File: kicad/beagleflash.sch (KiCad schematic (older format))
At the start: 22 parts, among them P1 SPI-8, P2 SPI-16, P3 BBB_P9, P4 BBB_P8, P5 EEPROM_PROG_EN, SW1 DIPS_02, U1 PAM2305AAB330, U2 74HC125, U3 CAT24C256W

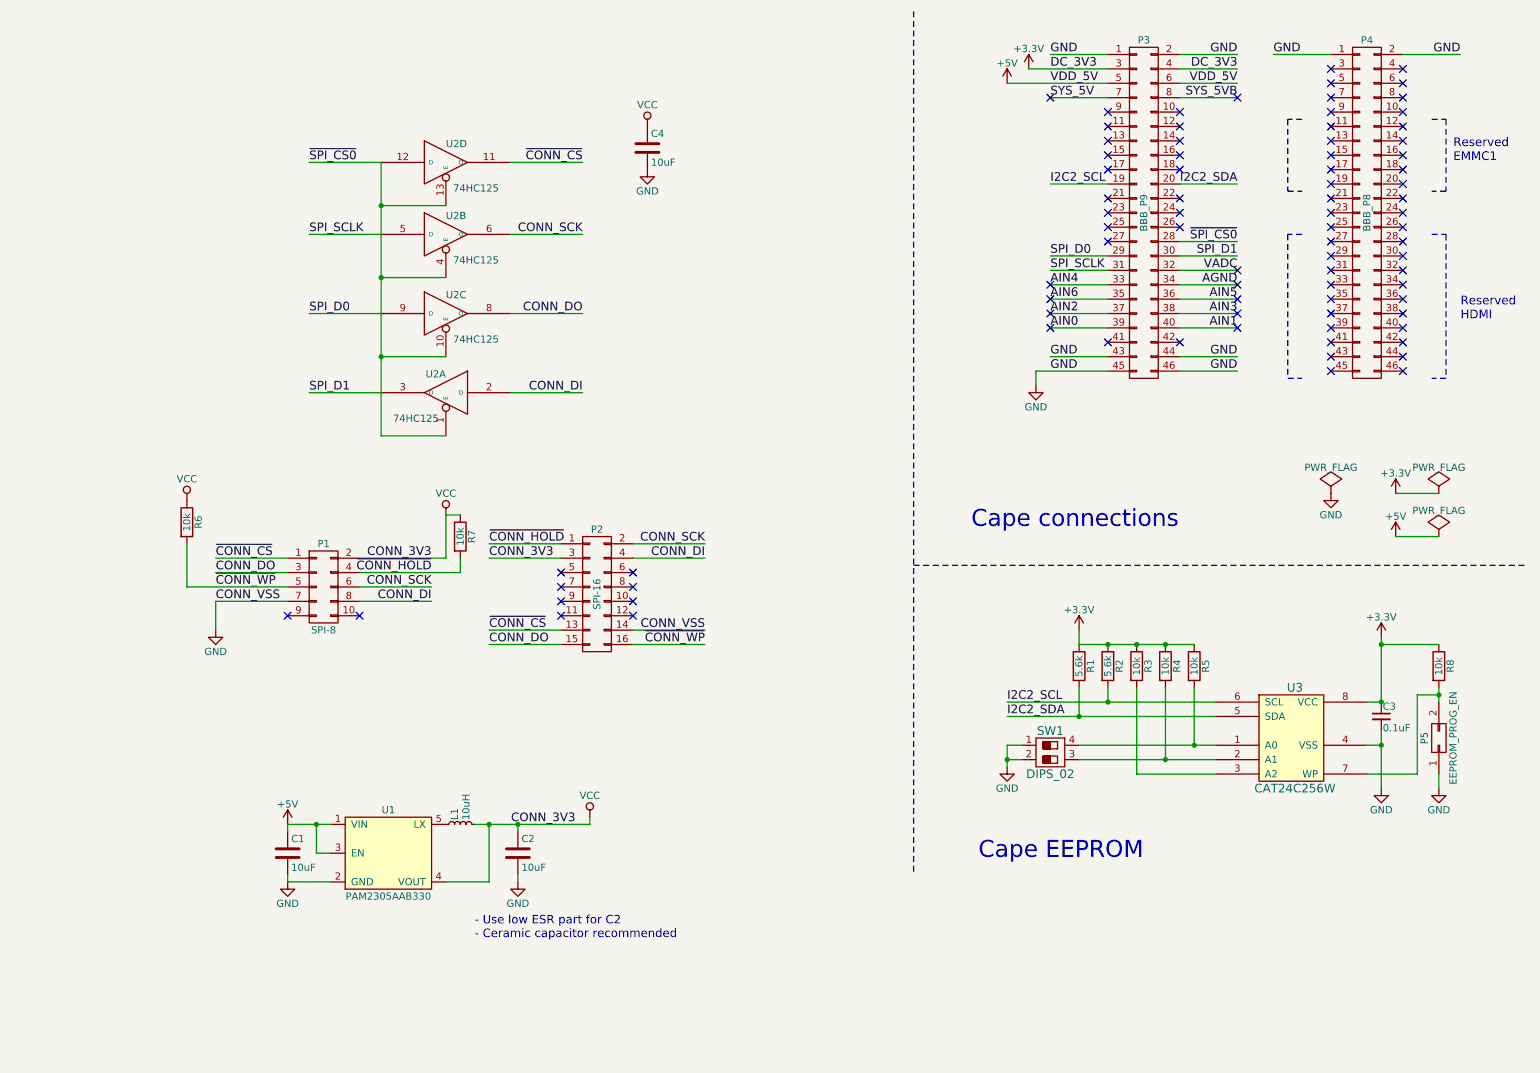
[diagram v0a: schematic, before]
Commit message: kicad: Add Revision 0.2 of beagleflash
Previous revision did not work because the MOSI and MISO pins were
swapped before the buffer. That's now fixed. Other changes include:
 - Replaced individual resistors around EEPROM with resistor array
 - Added silkscreen designators for SPI pinout on 10-pin header
 - Re-organized DC-DC regulator to have shorter current loops
 - Added exposed GND copper around mounting holes.

Signed-off-by: Alexandru Gagniuc <mr.nuke.me@gmail.com>
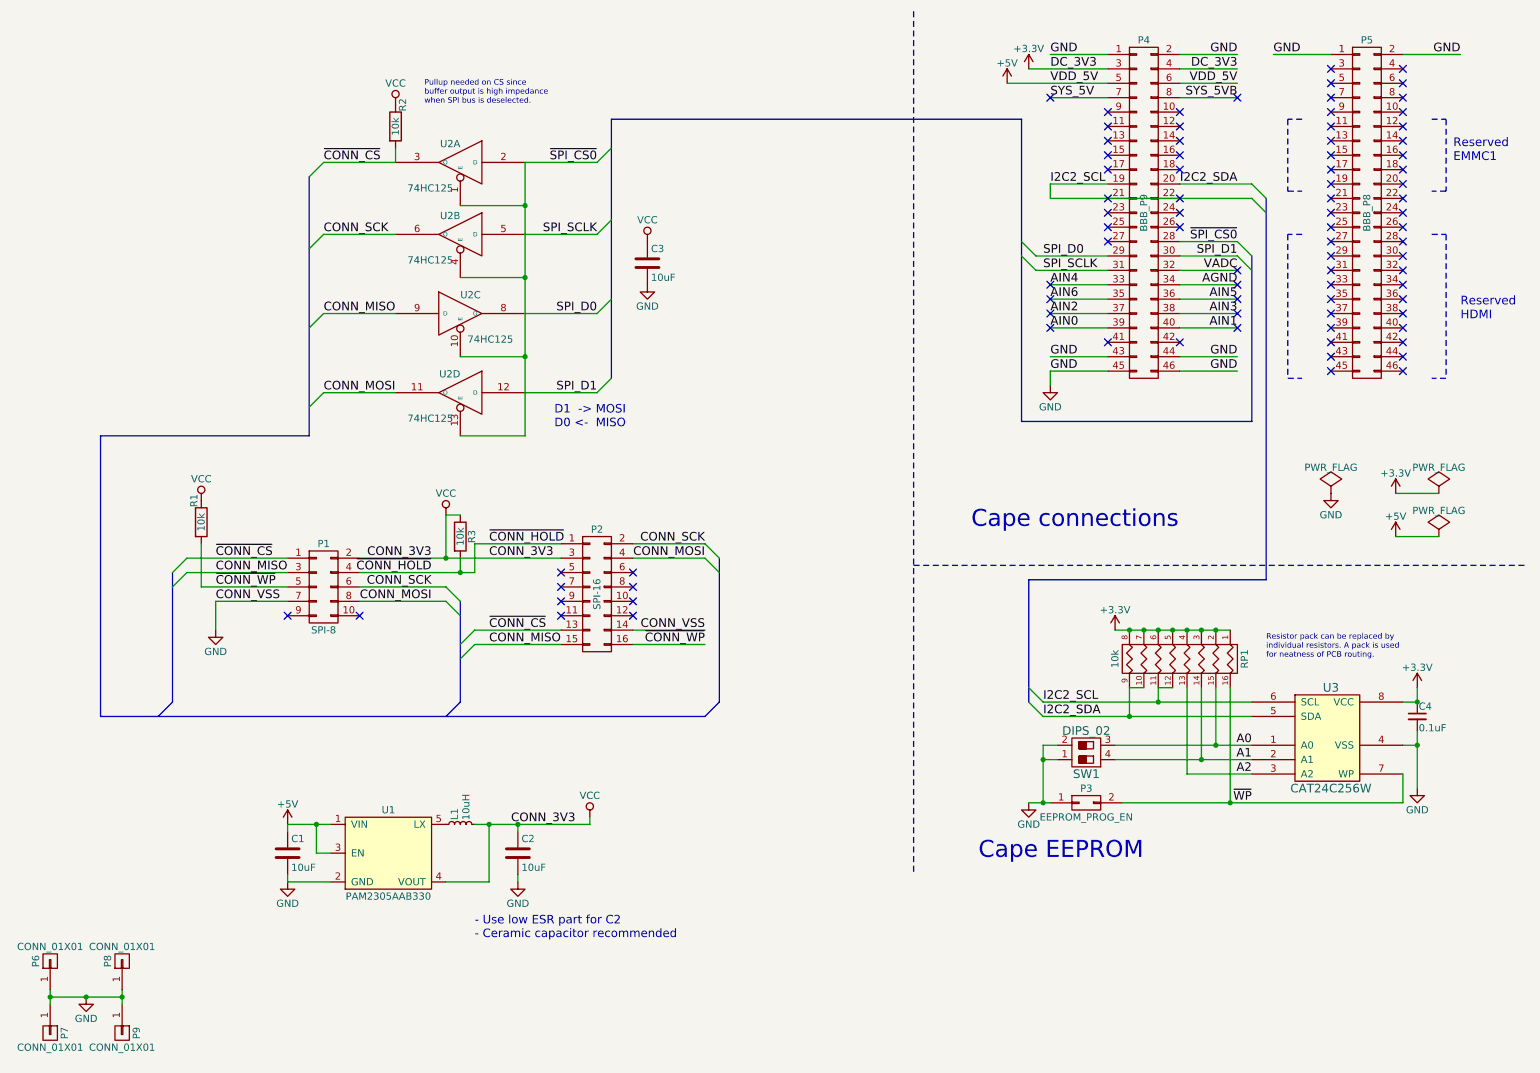
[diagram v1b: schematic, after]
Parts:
- removed R1: 5.6k, Resistors_SMD:R_0805, symbol R
- removed R3, R4, R5, R8: 10k, Resistors_SMD:R_0805, symbol R
- added P6, P7, P8, P9: CONN_01X01, Mounting_Holes:MountingHole_3.2mm_M3_ISO14580_Pad, symbol CONN_01X01
- added RP1: 10k, Housings_SOIC:SOIC-16_3.9x9.9mm_Pitch1.27mm, symbol R_PACK8
- L1: footprint Resistors_SMD:R_1812 -> Inductors_NEOSID:Neosid_Inductor_SM-NE45_SMD1812
- P1: footprint Pin_Headers:Pin_Header_Straight_2x05 -> Connect:IDC_Header_Straight_10pins
- P2: footprint Pin_Headers:Pin_Header_Straight_2x08 -> Connect:IDC_Header_Straight_16pins
- R2: value 5.6k -> 10k
- renumbered C4 to C3, C3 to C4, P5 to P3, P3 to P4, P4 to P5, R6 to R1, R7 to R3
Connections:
- net +3V3: now also RP1.1 (P1), RP1.2 (P2), RP1.3 (P3), RP1.4 (P4), RP1.5 (P5), RP1.6 (P6), RP1.7 (P7), RP1.8 (P8); no longer R2.1
- net GND: now also P6.1 (P1), P7.1 (P1), P8.1 (P1), P9.1 (P1)
- net I2C2_SCL: now also RP1.11 (R6), RP1.12 (R5); no longer R2.2
- net I2C2_SDA: now also RP1.10 (R7), RP1.9 (R8)
- net SPI_D0: now also U2.8 (O); no longer U2.9 (D)
- net SPI_D1: now also U2.12 (D); no longer U2.3 (O)
- net VCC: now also R2.1
- net ~CONN_CS: now also R2.2, U2.3 (O); no longer U2.11 (O)
- net ~SPI_CS0: now also U2.1 (E), U2.13 (E), U2.2 (D); no longer U2.1 (E), U2.12 (D), U2.13 (E)
- net A0: now reaches U3.1 (A0)
- net A0: now also SW1.3, RP1.15 (R2); no longer SW1.4
- net A1: now reaches U3.2 (A1)
- net A1: now also SW1.4, RP1.14 (R3); no longer SW1.3
- net A2: now reaches U3.3 (A2)
- net A2: now also RP1.13 (R4)
- net ~WP: now reaches P3.2 (P2), U3.7 (WP)
- net ~WP: now also RP1.16 (R1)
- net CONN_DI renamed CONN_MOSI
- net CONN_MOSI: now also U2.11 (O); no longer U2.2 (D)
- net CONN_DO renamed CONN_MISO
- net CONN_MISO: now also U2.9 (D); no longer U2.8 (O)
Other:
- note added: "D1 -> MOSI\nD0 <- MISO"
- note added: "Pullup needed on CS since\nbuffer output is high impedance\nwhen SPI bus is deselected."
- note added: "Resistor pack can be replaced by\nindividual resistors. A pack is used\nfor neatness of PCB routing."
- moved on the sheet: C3, C4, P3, R1, SW1, U2B, U2C, U3

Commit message: kicad: Update schematic to use KiCAD 5 symbol library
A lot has changed in kicad since beagleflash was originally designed.
KiCAD has a new library format, and it's preferrable to move all the
symbols to the new format before making any design improvements.

The is now a symbol for mounting holes with electrical connection:
    * Change mounting hole symbol from connector to MountingHole_Pad.

Signed-off-by: Alexandru Gagniuc <mr.nuke.me@gmail.com>
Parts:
- removed P6, P7, P8, P9: CONN_01X01, Mounting_Holes:MountingHole_3.2mm_M3_ISO14580_Pad, symbol CONN_01X01
- added H1, H2, H3, H4: M3, MountingHole:MountingHole_3.2mm_M3_ISO14580_Pad, symbol Mechanical:MountingHole_Pad
- C1, C2, C3: footprint Capacitors_SMD:C_0805 -> Capacitor_SMD:C_0805_2012Metric; symbol C -> Device:C
- C4: footprint Capacitors_SMD:C_0805 -> Capacitor_SMD:C_0805_2012Metric; symbol C_Small -> Device:C_Small
- L1: footprint Inductors_NEOSID:Neosid_Inductor_SM-NE45_SMD1812 -> Inductor_SMD:L_1812_4532Metric; symbol L_Small -> Device:L_Small
- P1: footprint Connect:IDC_Header_Straight_10pins -> Connector_IDC:IDC-Header_2x05_P2.54mm_Vertical; symbol CONN_02X05 -> Connector_Generic:Conn_02x05_Odd_Even
- P2: footprint Connect:IDC_Header_Straight_16pins -> Connector_IDC:IDC-Header_2x08_P2.54mm_Vertical; symbol CONN_02X08 -> Connector_Generic:Conn_02x08_Odd_Even
- P3: footprint Pin_Headers:Pin_Header_Angled_2x01 -> Connector_PinHeader_2.54mm:PinHeader_2x01_P2.54mm_Horizontal; symbol CONN_02X01 -> Connector_Generic:Conn_02x01
- P4, P5: footprint Pin_Headers:Pin_Header_Straight_2x23 -> Connector_PinHeader_2.54mm:PinHeader_2x23_P2.54mm_Vertical; symbol CONN_02X23 -> Connector_Generic:Conn_02x23_Odd_Even
- R1, R2, R3: footprint Resistors_SMD:R_0805 -> Resistor_SMD:R_0805_2012Metric; symbol R -> Device:R
- RP1: footprint Housings_SOIC:SOIC-16_3.9x9.9mm_Pitch1.27mm -> Package_SO:SOIC-16_3.9x9.9mm_P1.27mm; symbol R_PACK8 -> Device:R_Pack08
- SW1: footprint Buttons_Switches_ThroughHole:SW_DIP_x2_Slide -> Button_Switch_THT:SW_DIP_SPSTx02_Slide_9.78x7.26mm_W7.62mm_P2.54mm; symbol DIPS_02 -> Switch:SW_DIP_x02
- U1: footprint TO_SOT_Packages_SMD:SOT-23-5 -> Package_TO_SOT_SMD:TSOT-23-5; symbol SC189 -> Regulator_Switching:PAM2305AAB330
- U2: footprint Housings_SOIC:SOIC-14_3.9x8.7mm_Pitch1.27mm -> Package_SO:SOIC-14_3.9x8.7mm_P1.27mm; symbol 74LS125 -> 74xx:74LVC125
- U3: footprint Housings_SOIC:SOIC-8_3.9x4.9mm_Pitch1.27mm -> Package_SO:SOIC-8_3.9x4.9mm_P1.27mm; symbol CAT24C256W -> Memory_EEPROM:CAT24C256
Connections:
- net GND: now also H1.1, H2.1, H3.1, H4.1; no longer U2.7 (GND), U2.7 (GND), U2.7 (GND), U2.7 (GND)
- net VCC: no longer U2.14 (VCC), U2.14 (VCC), U2.14 (VCC), U2.14 (VCC)
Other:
- moved on the sheet: C4, U1, U3

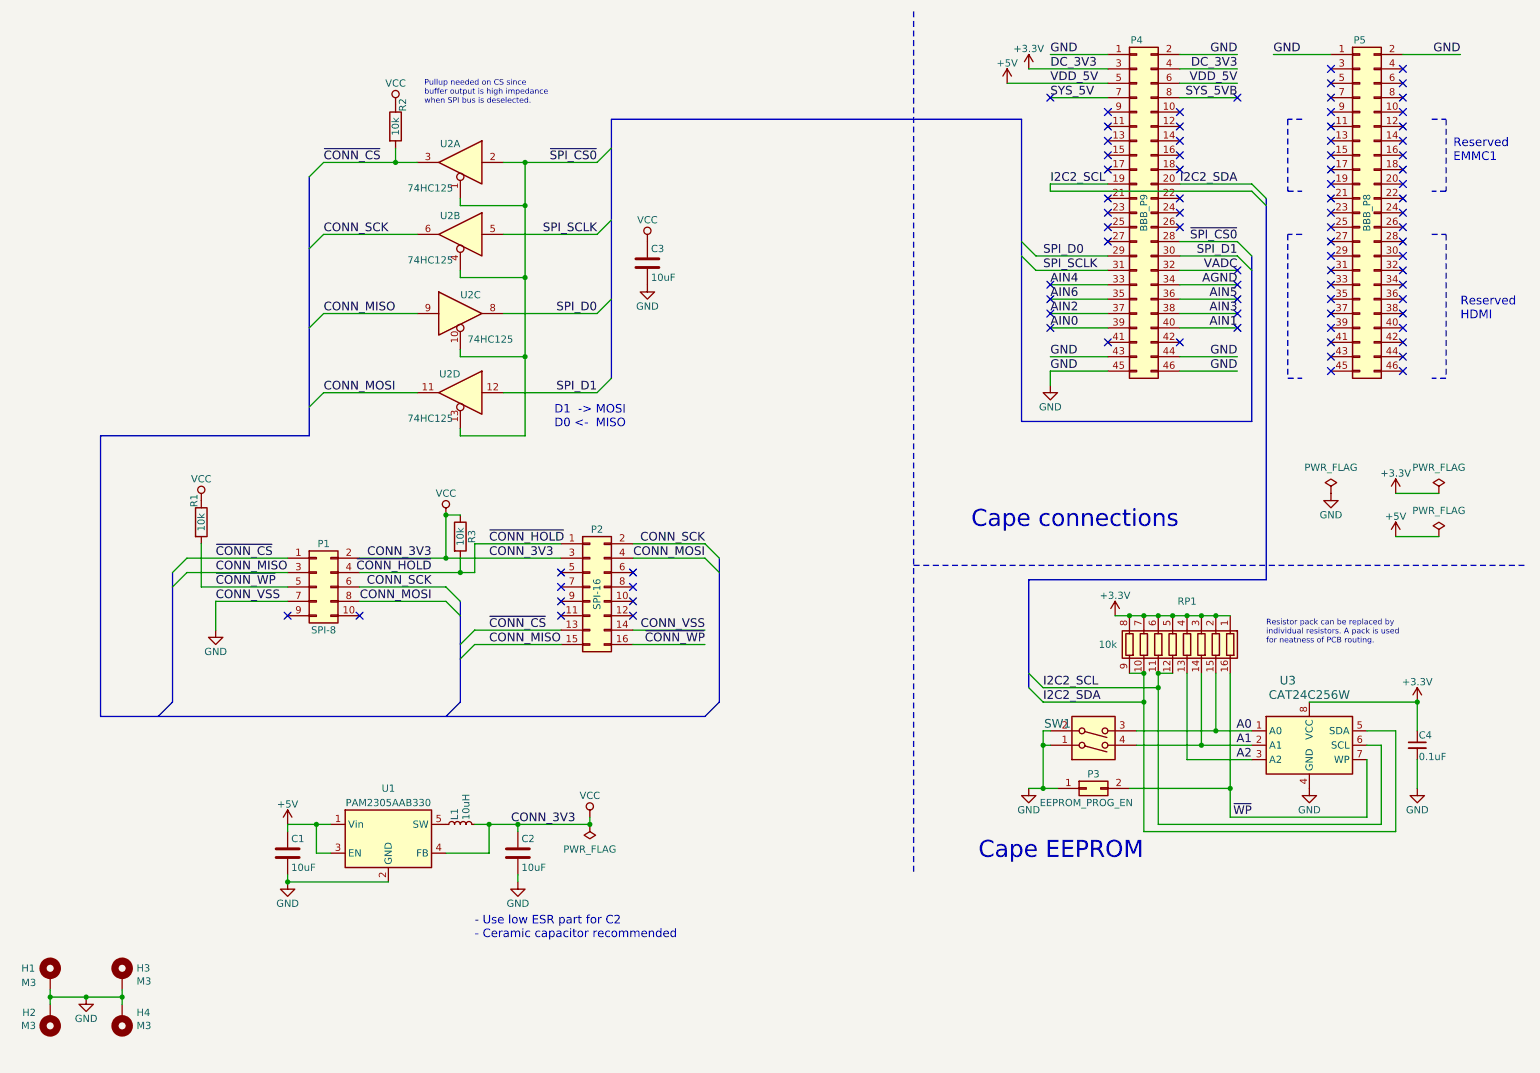
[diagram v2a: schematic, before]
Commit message: kicad: Add revision 0.3 schematic
Two incremental changes from rev 0.2:
 * Bring out debug UART to separate header
 * Add 1.8V programming option

Debug UART:
Sometimes, it may become necessarry to connect a debug UART to recover
a bricked beaglebone. Being able to do this without removing the cape
is preferrable.

1.8V programming option:
A larger number of new chips and boards operate at 1.8V. Not all
boards tolerate 3.3V, so a lower voltage option is necessarry.

Signed-off-by: Alexandru Gagniuc <mr.nuke.me@gmail.com>
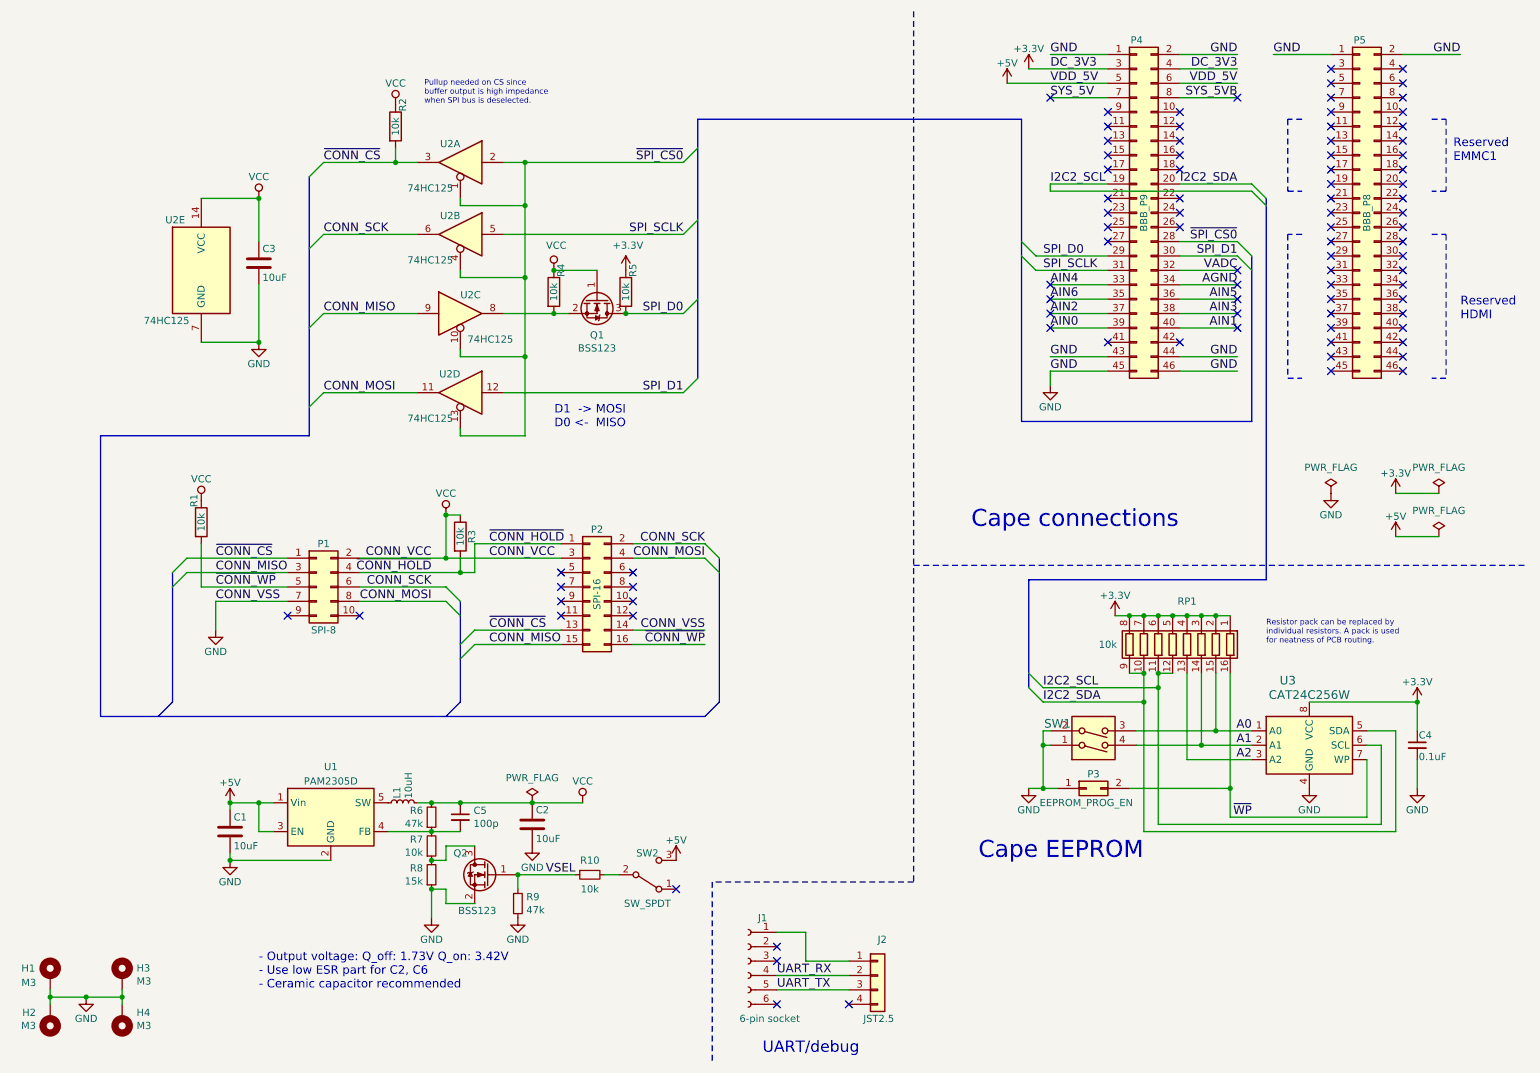
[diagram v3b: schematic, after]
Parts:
- added C5: 100p, Capacitor_SMD:C_0805_2012Metric, symbol Device:C_Small
- added J1: 6-pin socket, Connector_PinHeader_2.54mm:PinHeader_1x06_P2.54mm_Vertical, symbol Connector:Conn_01x06_Female
- added J2: JST2.5, Connector_JST:JST_XH_B04B-XH-A_1x04_P2.50mm_Vertical, symbol Connector_Generic:Conn_01x04
- added Q1, Q2: BSS123, Package_TO_SOT_SMD:SOT-23, symbol Device:Q_NMOS_GSD
- added R10, R7: 10k, Resistor_SMD:R_0805_2012Metric, symbol Device:R_Small
- added R4, R5: 10k, Resistor_SMD:R_0805_2012Metric, symbol Device:R
- added R6, R9: 47k, Resistor_SMD:R_0805_2012Metric, symbol Device:R_Small
- added R8: 15k, Resistor_SMD:R_0805_2012Metric, symbol Device:R_Small
- added SW2: SW_SPDT, Connector_PinHeader_2.54mm:PinHeader_1x03_P2.54mm_Horizontal, symbol Switch:SW_SPDT
- added unit 5 of U2
- U1: value PAM2305AAB330 -> PAM2305D
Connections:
- net +3V3: now also R5.1
- net +5V: now also SW2.3 (C)
- net GND: now also Q2.2 (S), R8.1, R9.2, U2.7 (GND)
- net SPI_D0: now also Q1.3 (D), R5.2; no longer U2.8
- net VCC: now also C5.1, Q1.1 (G), R4.1, R6.2, U2.14 (VCC); no longer U1.4 (FB)
- new net: Q1.2 (S), R4.2, U2.8
- new net: C5.2, R6.1, R7.2, U1.4 (FB)
- new net: J1.1 (Pin_1), J2.1 (Pin_1)
- new net: R10.2, SW2.2 (B)
- new net: Q2.3 (D), R7.1, R8.2
- new net UART_RX: J1.4 (Pin_4), J2.2 (Pin_2)
- new net UART_TX: J1.5 (Pin_5), J2.3 (Pin_3)
- new net VSEL: Q2.1 (G), R10.1, R9.1
- no-connect marks 84 -> 89
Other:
- note added: "- Output voltage: Q_off: 1.73V Q_on: 3.42V\n- Use low ESR part for C2, C6\n- Ceramic capacitor recommended"
- note added: "UART/debug"
- note removed: "- Use low ESR part for C2\n- Ceramic capacitor recommended"
- moved on the sheet: C1, C2, C3, L1, U1
